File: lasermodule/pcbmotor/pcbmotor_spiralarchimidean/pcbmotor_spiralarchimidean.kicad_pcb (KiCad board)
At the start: 4 copper layers, 45.5 x 43.4 mm, 5 parts, among them J1 Conn_01x03, J2 Conn_01x01, J3 Conn_01x01, J4 Conn_01x01, J5 Conn_01x01

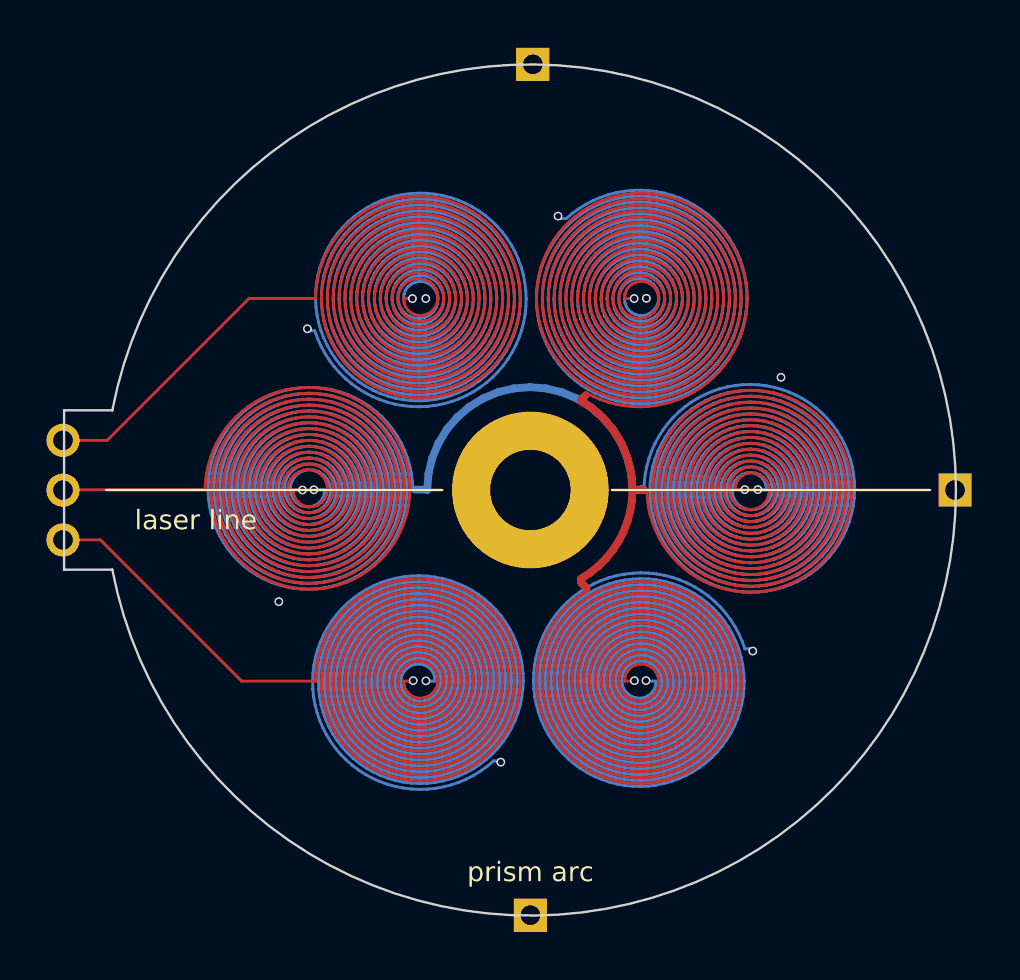
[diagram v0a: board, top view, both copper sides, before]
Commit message: changes to reduce prices pcbway
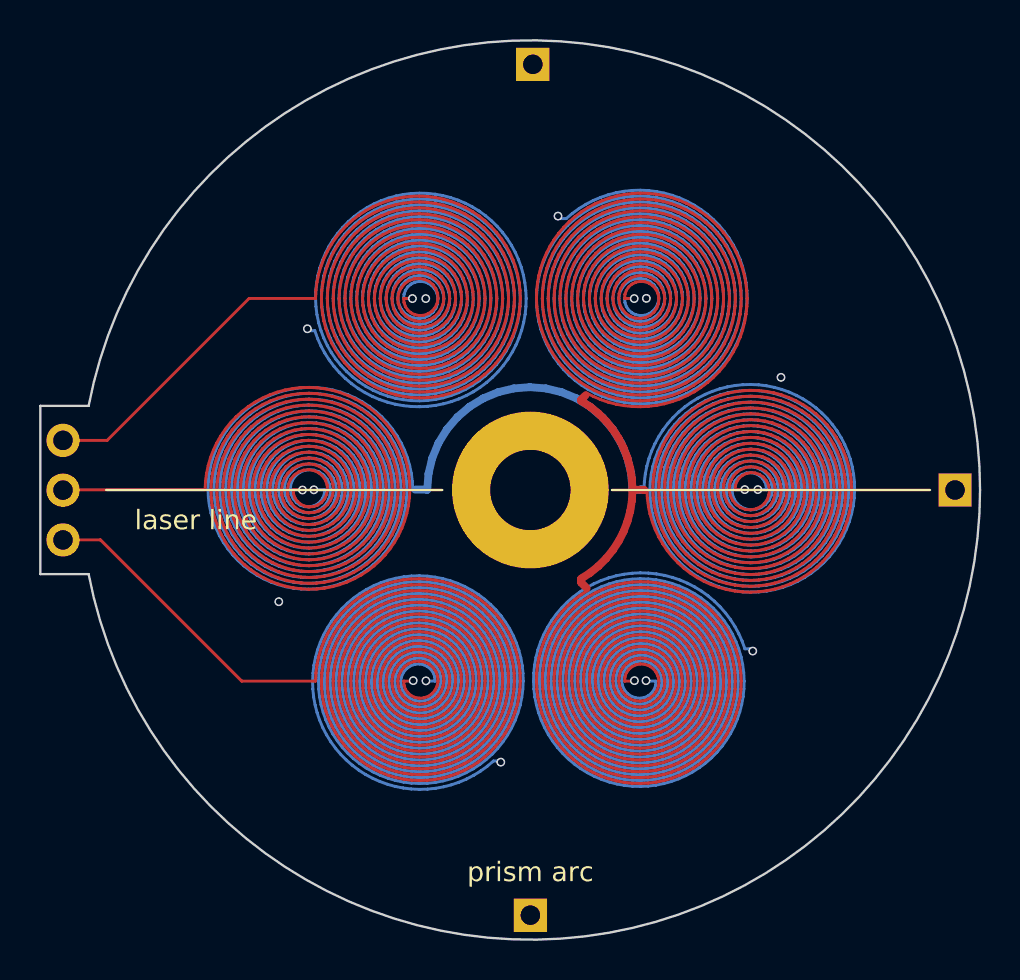
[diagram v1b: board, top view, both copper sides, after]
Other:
- board size 45.5 x 43.4 mm -> 48 x 45.9 mm
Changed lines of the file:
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@@
 	)
 	(gr_line
-		(start 80.972 118.21)
-		(end 80.972 110.082)
+		(start 79.763332 118.440232)
+		(end 79.763332 109.851768)
 		(stroke
 			(width 0.12)
@@
 	)
 	(gr_arc
-		(start 83.436 110.082)
-		(mid 126.491599 114.146)
-		(end 83.436 118.21)
+		(start 82.227332 109.851768)
+		(mid 127.722 114.146)
+		(end 82.227332 118.440232)
 		(stroke
 			(width 0.12)
@@
 	)
 	(gr_line
-		(start 80.972 110.082)
-		(end 83.436 110.082)
+		(start 79.763332 109.851768)
+		(end 82.227332 109.851768)
 		(stroke
 			(width 0.12)
@@
 	)
 	(gr_line
-		(start 83.436 118.21)
-		(end 80.972 118.21)
+		(start 82.227332 118.440232)
+		(end 79.763332 118.440232)
 		(stroke
 			(width 0.12)
